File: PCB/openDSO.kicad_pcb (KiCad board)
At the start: 2 copper layers, 1 part, among them J1 Z_TURN_Lite

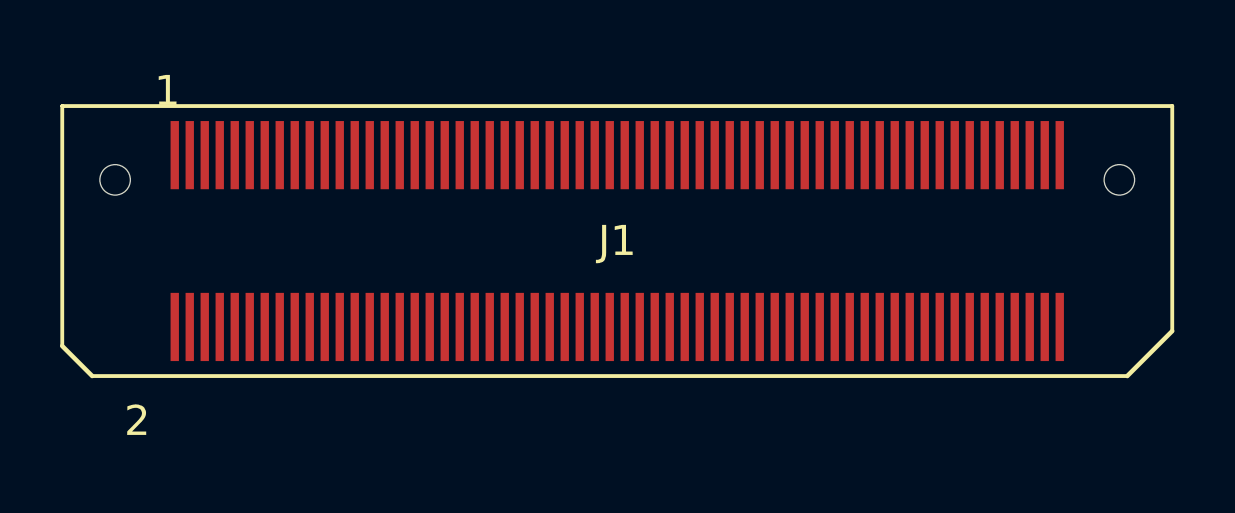
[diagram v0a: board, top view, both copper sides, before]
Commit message: fix Zturn footprint
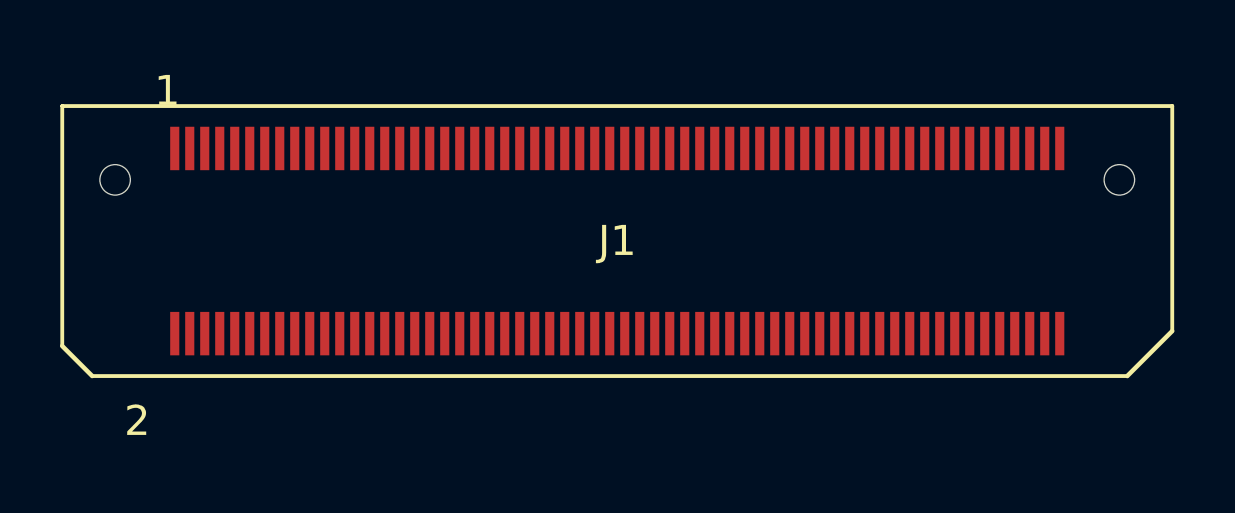
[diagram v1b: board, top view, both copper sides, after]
